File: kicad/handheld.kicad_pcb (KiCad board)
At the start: 4 copper layers, 240 x 76 mm, 95 parts, among them J1 Conn_01x08, J2 61300311121, J3 AVR-PDI-6, J4 UE27AC54100, SW1 HOLD, SW2 PAUSE, SW3 SDROP, SW4 HDROP, SW5 ROTR, SW6 RIGHT, SW7 ROTL, SW8 RIGHT, U1 TFBS4711, U10 DMN601, U11 NSI45015, U12 SN54LV574, U13 P-FET, U14 NSI45015, U15 DMN601, U16 NSI45015, U17 NSI45015, U18 DMN601, U19 P-FET, U2 ATxmega64C3-AU, U20 NSI45015, U21 74HCT595, U22 NSI45015, U23 DMN601, U24 NSI45015, U25 P-FET, U26 NSI45015, U27 DMN601, U28 NSI45015, U29 SN54LV574, U3 P-FET, U30 NSI45015, U31 DMN601, U32 NSI45015, U33 P-FET, U34 NSI45015, U35 DMN601, U36 NSI45015, U37 NSI45015, U38 P-FET, U39 DMN601, U4 LM3671MF-3.3, U40 NSI45015, U41 NSI45015, U42 DMN601, U43 NSI45015, U44 SN54LV574, U45 74HCT595, U46 P-FET, U47 NSI45015, U48 DMN601, U49 NSI45015, U5 NSI45015, U50 NSI45015, U51 DMN601, U52 P-FET, U53 NSI45015, U6 P-FET, U7 DMN601, U8 NSI45015, U9 NSI45015

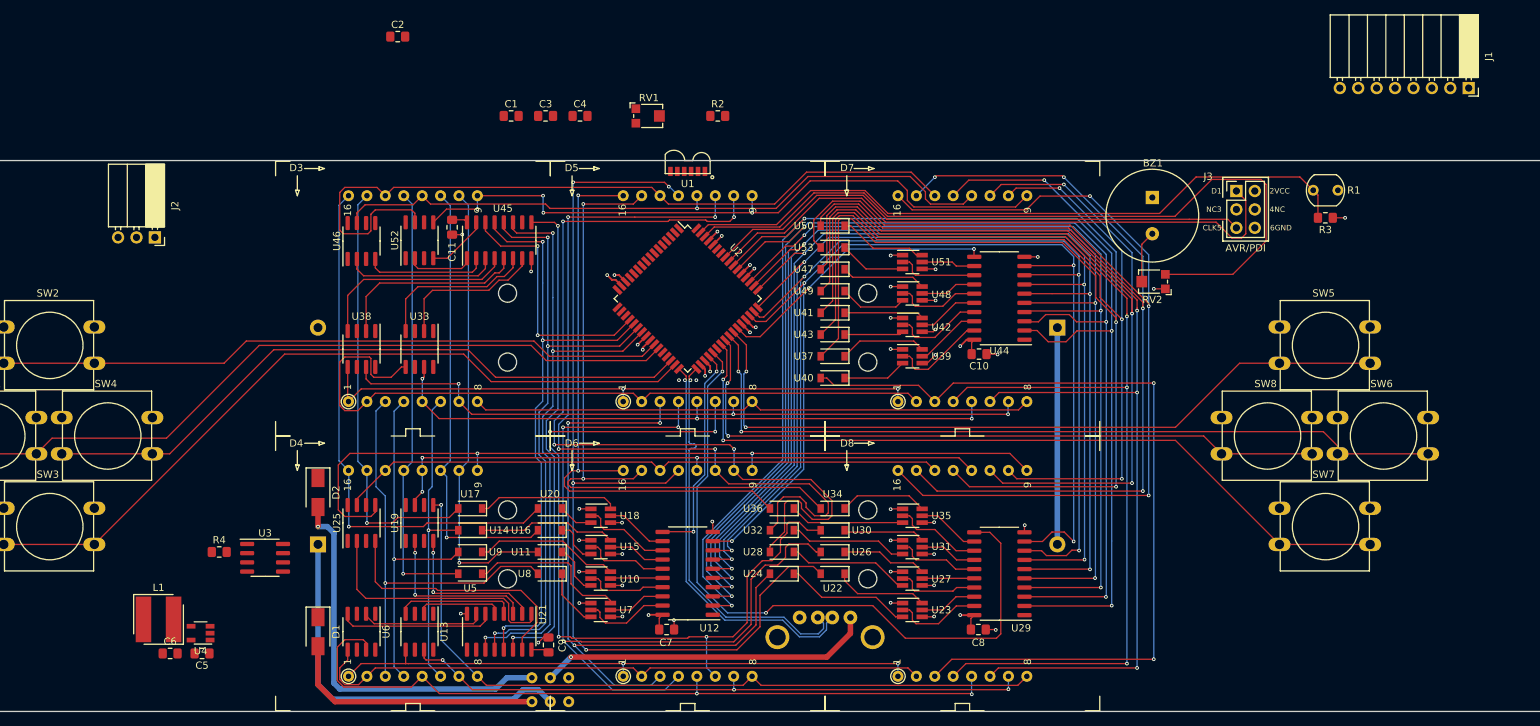
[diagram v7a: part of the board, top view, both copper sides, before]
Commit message: Added power net and buck converter
Also wired up Ir transceiver.
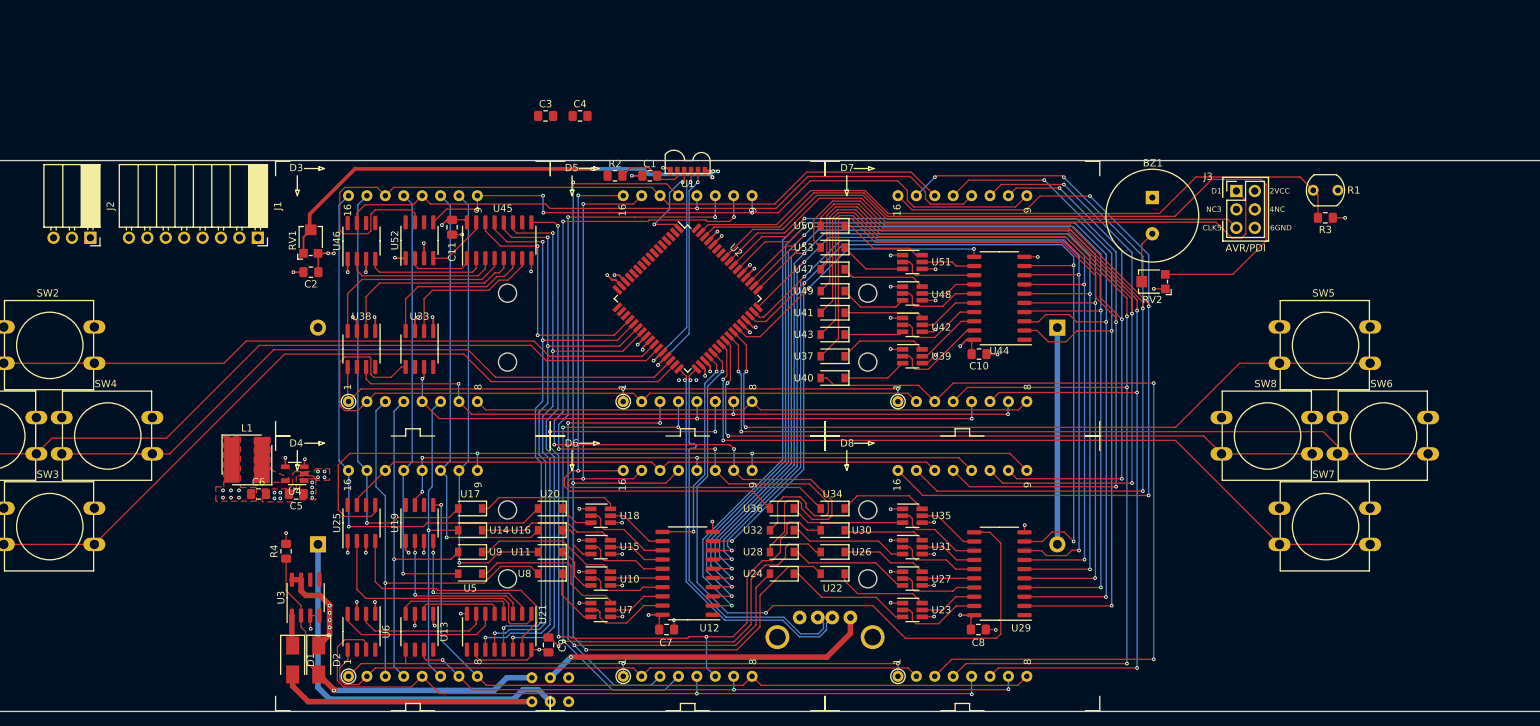
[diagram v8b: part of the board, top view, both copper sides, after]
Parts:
- moved J1 168.3 mm to (93.1, 74.2)
- moved RV1 49.7 mm to (100.4, 74.6), turned to 90 degrees
- moved C2 34.6 mm to (100.4, 79.0), turned to 180 degrees
- moved U4 25.6 mm to (98.2, 106.8)
- moved C5 25.6 mm to (98.4, 109.6)
- moved C6 25.2 mm to (93.2, 109.6)
- moved L1 25.2 mm to (91.6, 104.9)
- moved D2 23.1 mm to (101.5, 132.5)
- moved C1 20.8 mm to (147.2, 65.7)
- moved R2 16.4 mm to (142.4, 65.7)
- moved R4 9.23 mm to (97.0, 117.5), turned to 90 degrees
- moved J2 8.90 mm to (70.0, 74.2)
- moved U3 7.85 mm to (99.7, 123.9), turned to 90 degrees
- moved D1 5.24 mm to (97.9, 132.5)
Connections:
- net Net-(L1-Pad2) renamed /power/SW
- U1 pad 4: Net-(U1-Pad4) -> /IrSD
- U2 pad 1: Net-(U2-Pad1) -> /IrSD
- U2 pad 16: Net-(U1-Pad4) -> Net-(U2-Pad16)
- U2 pad 18: /IrRX -> /RX
- U2 pad 19: /IrTX -> /TX
- U2 pad 28: /RX -> /IrRX
- U2 pad 29: /TX -> /IrTX
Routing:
- net Net-(RV1-Pad1): track 0.00 -> 67.0 mm, vias 0 -> 3
- net U_PWR: track 4.71 -> 64.7 mm, vias 0 -> 30
- net /IrTX: track 0.00 -> 30.7 mm, vias 0 -> 2
- net /IrRX: track 0.00 -> 29.9 mm, vias 0 -> 2
- net /IrSD: track 0.00 -> 12.9 mm, vias 0 -> 2
- net Net-(C1-Pad2): track 0.00 -> 9.57 mm
- net GND: track 69.2 -> 78.1 mm, vias 44 -> 57
- net Net-(D2-Pad2): track 54.3 -> 48.9 mm
- net Net-(D1-Pad1): track 0.00 -> 4.17 mm
- net Net-(U21-Pad7): track 17.1 -> 18.7 mm
- net Net-(U21-Pad6): track 21.6 -> 22.9 mm
- net VDD: track 24.2 -> 25.4 mm, vias 9 -> 16
- net /Matrix Driver/COL8: vias 4 -> 3
- added copper zone on F.Cu, net /power/SW
- added copper zone on F.Cu, net GND
- added copper zone on F.Cu, net U_PWR
- added copper zone on In2.Cu.Pwr, net U_PWR
- added copper zone on F.Cu, net VDD
